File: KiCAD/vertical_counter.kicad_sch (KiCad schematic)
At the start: 14 parts, among them U10 74HC04, U12 74HC32, U15 74HC161, U16 74HC161, U17 74HC161, U18 74HC04, U19 74HC04, U20 74HC133, U21 74HC133, U22 74HC133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

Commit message: finished schematics and footprint assignments; need to figure out +5v connection issue
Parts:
- added unit 3 of U24
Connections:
- net +5V: now also U24.16 (VCC)
- net GND: now also U24.8 (GND)
- net j_addr4 renamed i_addr4
- net j_addr5 renamed i_addr5
- net j_addr6 renamed i_addr6
- net j_addr7 renamed i_addr7
- no-connect marks 4 -> 2
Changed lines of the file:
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@@
 	)
 	(junction
+		(at 255.27 30.48)
+		(diameter 0)
+		(color 0 0 0 0)
+	)
+	(junction
 		(at 77.47 162.56)
 		(diameter 0)
@@
 	)
 	(junction
+		(at 255.27 55.88)
+		(diameter 0)
+		(color 0 0 0 0)
+	)
+	(junction
 		(at 77.47 124.46)
 		(diameter 0)
@@
 	)
 	(no_connect
-		(at 154.94 134.62)
-	)
-	(no_connect
-		(at 151.13 138.43)
-	)
-	(no_connect
-		(at 151.13 172.72)
+		(at 168.91 175.26)
 	)
 	(no_connect
@@
 	(wire
 		(pts
+			(xy 255.27 30.48) (xy 270.51 30.48)
+		)
+		(stroke
+			(width 0)
+			(type default)
+		)
+	)
+	(wire
+		(pts
 			(xy 209.55 55.88) (xy 224.79 55.88)
 		)
@@
 	(wire
 		(pts
+			(xy 270.51 30.48) (xy 270.51 33.02)
+		)
+		(stroke
+			(width 0)
+			(type default)
+		)
+	)
+	(wire
+		(pts
 			(xy 179.07 55.88) (xy 194.31 55.88)
 		)
@@
 		)
 	)
+	(wire
+		(pts
+			(xy 270.51 53.34) (xy 270.51 55.88)
+		)
+		(stroke
+			(width 0)
+			(type default)
+		)
+	)
 	(bus
 		(pts
@@
 	(wire
 		(pts
+			(xy 270.51 55.88) (xy 255.27 55.88)
+		)
+		(stroke
+			(width 0)
+			(type default)
+		)
+	)
+	(wire
+		(pts
 			(xy 245.11 191.77) (xy 259.08 191.77)
 		)
@@
 		)
 	)
-	(label "j_addr5"
+	(label "i_addr5"
 		(at 245.11 194.31 0)
 		(effects
@@
 		)
 	)
-	(label "j_addr3"
+	(label "i_addr3"
 		(at 247.65 139.7 0)
 		(effects
@@
 		)
 	)
-	(label "j_addr0"
+	(label "i_addr0"
 		(at 247.65 132.08 0)
 		(effects
@@
 		)
 	)
-	(label "j_addr1"
+	(label "i_addr1"
 		(at 247.65 134.62 0)
 		(effects
@@
 		)
 	)
-	(label "j_addr2"
+	(label "i_addr2"
 		(at 247.65 137.16 0)
 		(effects
@@
 		)
 	)
-	(label "j_addr4"
+	(label "i_addr4"
 		(at 245.11 191.77 0)
 		(effects
@@
 		)
 	)
-	(label "j_addr7"
+	(label "i_addr7"
 		(at 245.11 199.39 0)
 		(effects
@@
 		)
 	)
-	(label "j_addr6"
+	(label "i_addr6"
 		(at 245.11 196.85 0)
 		(effects
@@
 		)
 	)
-	(hierarchical_label "j_addr[0..7]"
+	(hierarchical_label "i_addr[0..7]"
 		(shape output)
 		(at 290.83 201.93 0)
@@
 				)
 			)
+		)
+	)
+	(symbol
+		(lib_id "74xx:74LS112")
+		(at 270.51 43.18 0)
+		(unit 3)
+		(exclude_from_sim no)
+		(in_bom yes)
+		(on_board yes)
+		(dnp no)
+		(fields_autoplaced yes)
+		(property "Reference" "U24"
+			(at 272.6533 33.02 0)
+			(effects
+				(font
+					(size 1.27 1.27)
+				)
+				(justify left)
+			)
+		)
+		(property "Value" "74HC112"
+			(at 272.6533 35.56 0)
+			(effects
+				(font
+					(size 1.27 1.27)
+				)
+				(justify left)
+			)
+		)
+		(property "Footprint" "Package_DIP:DIP-16_W7.62mm"
+			(at 270.51 43.18 0)
+			(effects
+				(font
+					(size 1.27 1.27)
+				)
+				(hide yes)
+			)
+		)
+		(property "Datasheet" "http://www.ti.com/lit/gpn/sn74LS112"
+			(at 270.51 43.18 0)
+			(effects
+				(font
+					(size 1.27 1.27)
+				)
+				(hide yes)
+			)
+		)
+		(property "Description" "dual JK Flip-Flop, Set & Reset"
+			(at 270.51 43.18 0)
+			(effects
+				(font
+					(size 1.27 1.27)
+				)
+				(hide yes)
+			)
+		)
+		(pin "1"
+		)
+		(pin "12"
+		)
+		(pin "5"
+		)
+		(pin "3"
+		)
+		(pin "15"
+		)
+		(pin "2"
+		)
+		(pin "11"
+		)
+		(pin "4"
+		)
+		(pin "10"
+		)
+		(pin "14"
+		)
+		(pin "7"
+		)
+		(pin "6"
+		)
+		(pin "13"
+		)
+		(pin "8"
+		)
+		(pin "16"
+		)
+		(pin "9"
+		)
+		(instances
+			(project "vga_video_card"
+				(path "/53ebbfbe-eaa1-4706-acc1-611a99db7179/318d78f1-f69a-43bc-862b-642862639a11"
+					(reference "U24")
+					(unit 3)
+				)
+			)

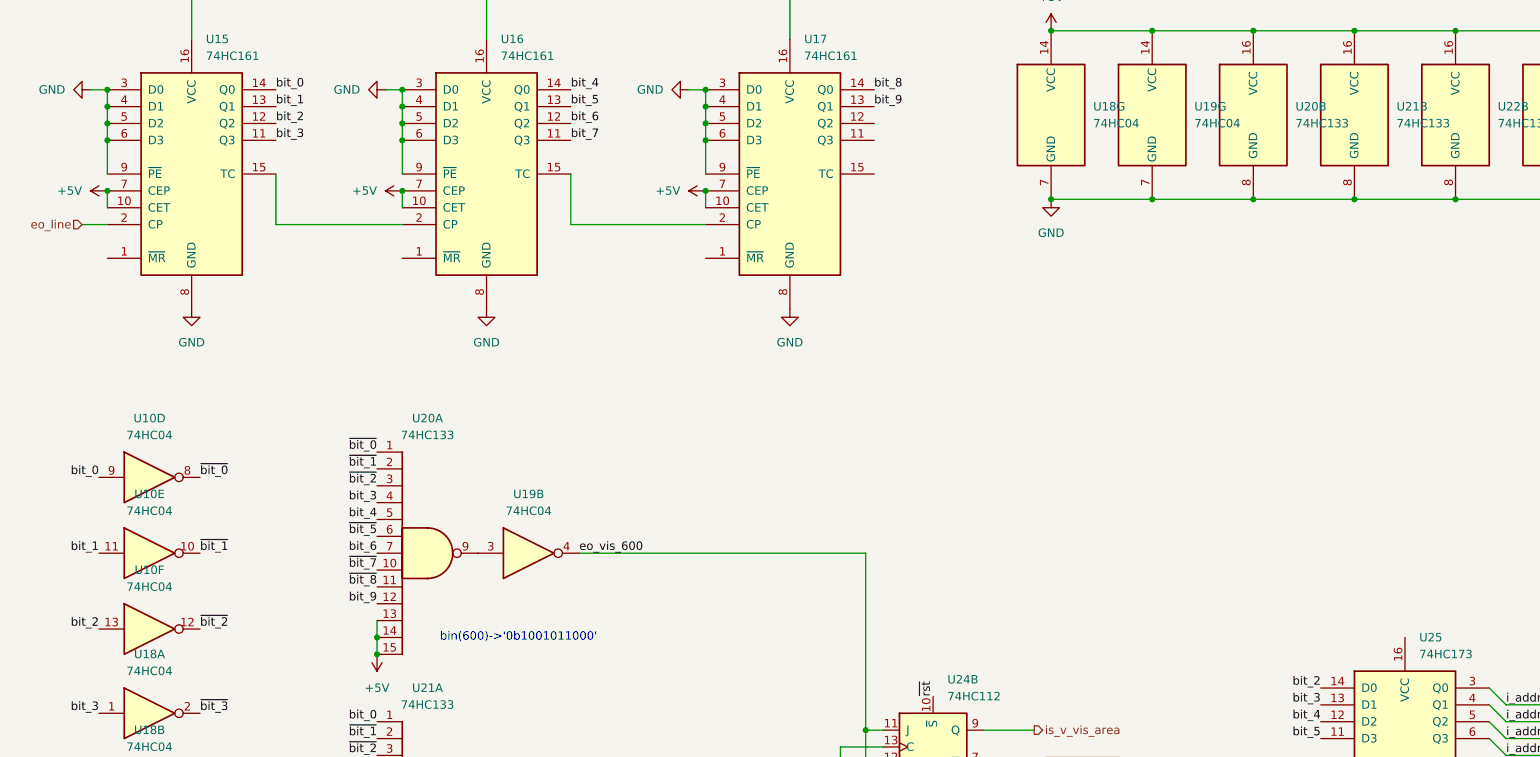
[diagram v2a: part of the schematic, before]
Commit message: fix multiple ERCs that made RAM addrs not connecting
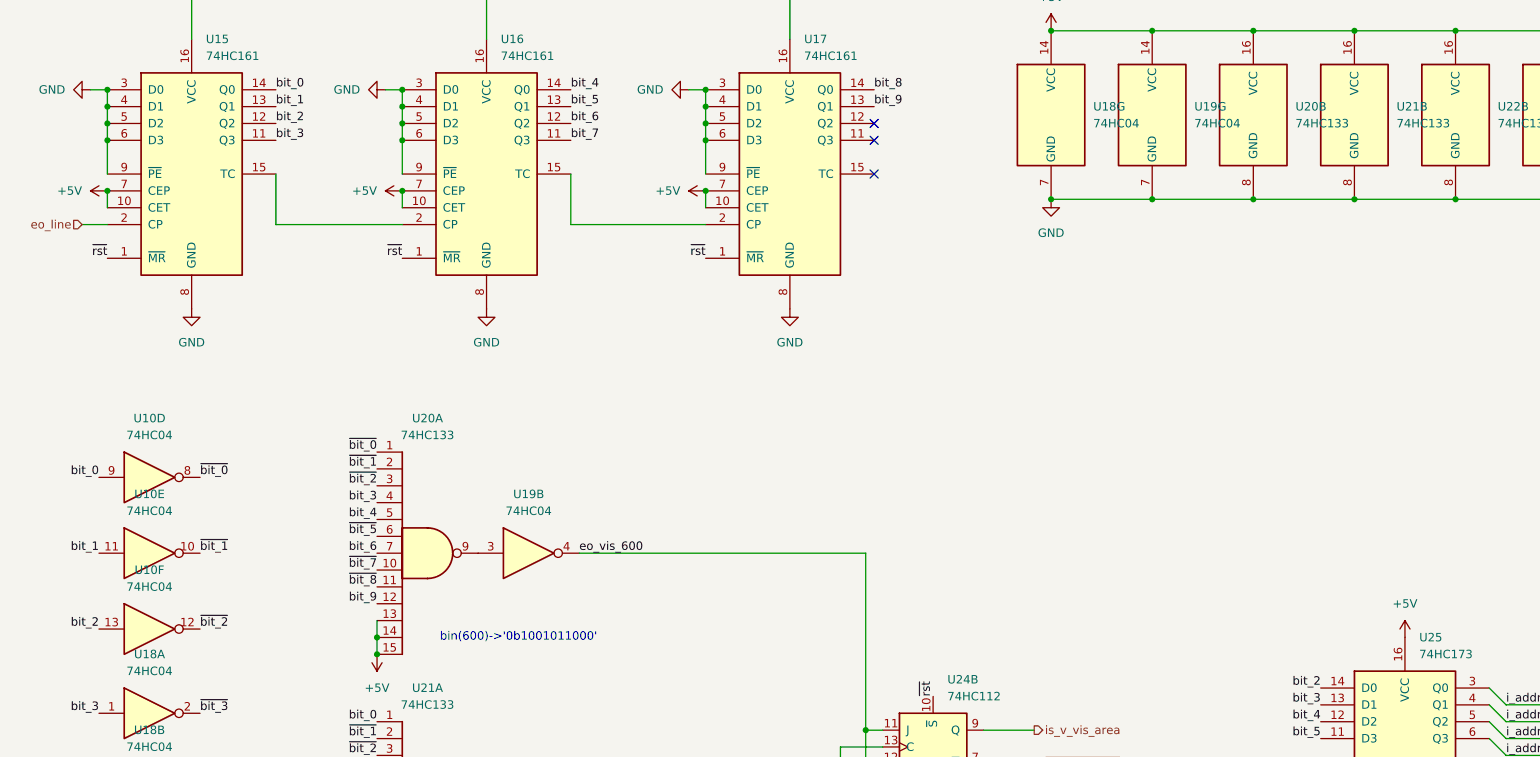
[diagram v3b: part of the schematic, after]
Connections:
- net +5V: now also U25.16 (VCC)
- net ~{rst}: now also U15.1 (~{MR}), U16.1 (~{MR}), U17.1 (~{MR})
- no-connect marks 2 -> 5
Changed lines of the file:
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@@
 	)
 	(no_connect
+		(at 152.4 44.45)
+	)
+	(no_connect
+		(at 152.4 52.07)
+	)
+	(no_connect
+		(at 152.4 46.99)
+	)
+	(no_connect
 		(at 222.25 209.55)
 	)
@@
 		)
 	)
+	(label "~{rst}"
+		(at 81.28 64.77 180)
+		(effects
+			(font
+				(size 1.27 1.27)
+			)
+			(justify right bottom)
+		)
+	)
 	(label "bit_0"
 		(at 77.47 176.53 180)
@@
 		)
 	)
+	(label "~{rst}"
+		(at 36.83 64.77 180)
+		(effects
+			(font
+				(size 1.27 1.27)
+			)
+			(justify right bottom)
+		)
+	)
 	(label "bit_8"
 		(at 219.71 196.85 180)
@@
 		)
 	)
+	(label "~{rst}"
+		(at 127 64.77 180)
+		(effects
+			(font
+				(size 1.27 1.27)
+			)
+			(justify right bottom)
+		)
+	)
 	(label "bit_6"
 		(at 106.68 44.45 0)
@@
 					(unit 1)
 				)
+			)
+		)
+	)
+	(symbol
+		(lib_id "power:+5V")
+		(at 232.41 121.92 0)
+		(unit 1)
+		(exclude_from_sim no)
+		(in_bom yes)
+		(on_board yes)
+		(dnp no)
+		(fields_autoplaced yes)
+		(property "Reference" "#PWR0119"
+			(at 232.41 125.73 0)
+			(effects
+				(font
+					(size 1.27 1.27)
+				)
+				(hide yes)
+			)
+		)
+		(property "Value" "+5V"
+			(at 232.41 116.84 0)
+			(effects
+				(font
+					(size 1.27 1.27)
+				)
+			)
+		)
+		(property "Footprint" ""
+			(at 232.41 121.92 0)
+			(effects
+				(font
+					(size 1.27 1.27)
+				)
+				(hide yes)
+			)
+		)
+		(property "Datasheet" ""
+			(at 232.41 121.92 0)
+			(effects
+				(font
+					(size 1.27 1.27)
+				)
+				(hide yes)
+			)
+		)
+		(property "Description" "Power symbol creates a global label with name \"+5V\""
+			(at 232.41 121.92 0)
+			(effects
+				(font
+					(size 1.27 1.27)
+				)
+				(hide yes)
+			)
+		)
+		(pin "1"
+		)
+		(instances
+			(project ""
+				(path "/53ebbfbe-eaa1-4706-acc1-611a99db7179/318d78f1-f69a-43bc-862b-642862639a11"
+					(reference "#PWR0119")
+					(unit 1)
+				)

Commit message: clean up; resolve ERC warnings
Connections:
- net i_addr0: now also U25.3 (Q0)
- net i_addr1: now also U25.4 (Q1)
- net i_addr2: now also U25.5 (Q2)
- net i_addr3: now also U25.6 (Q3)

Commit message: resolved most ERC errors
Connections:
- no-connect marks 5 -> 4
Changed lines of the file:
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@@
 		(at 152.4 46.99)
-	)
-	(no_connect
-		(at 222.25 209.55)
 	)
 	(bus_entry

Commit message: updated KiCAD todos
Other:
- note added: "TODO: PE should be disabled"
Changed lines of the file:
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@@
+		)
+	)
+	(text "TODO: PE should be disabled"
+		(exclude_from_sim no)
+		(at 29.464 28.956 0)
+		(effects
+			(font
+				(size 1.27 1.27)
+			)
 		)
 	)

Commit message: schematics disabled PE
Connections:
- net +5V: now also U15.9 (~{PE}), U16.9 (~{PE}), U17.9 (~{PE})
- net GND: no longer U15.9 (~{PE}), U16.9 (~{PE}), U17.9 (~{PE})
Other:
- note removed: "TODO: PE should be disabled"
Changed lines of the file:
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@@
-		)
-	)
-	(text "TODO: PE should be disabled"
-		(exclude_from_sim no)
-		(at 29.464 28.956 0)
-		(effects
-			(font
-				(size 1.27 1.27)
-			)
 		)
 	)
@@
 	)
 	(junction
-		(at 81.28 46.99)
-		(diameter 0)
-		(color 0 0 0 0)
-	)
-	(junction
-		(at 36.83 46.99)
-		(diameter 0)
-		(color 0 0 0 0)
-	)
-	(junction
 		(at 224.79 30.48)
 		(diameter 0)
@@
 	(junction
 		(at 219.71 205.74)
-		(diameter 0)
-		(color 0 0 0 0)
-	)
-	(junction
-		(at 127 46.99)
 		(diameter 0)
 		(color 0 0 0 0)
@@
 	(wire
 		(pts
+			(xy 127 52.07) (xy 127 54.61)
+		)
+		(stroke
+			(width 0)
+			(type default)
+		)
+	)
+	(wire
+		(pts
 			(xy 245.11 134.62) (xy 259.08 134.62)
 		)
@@
 	(wire
 		(pts
-			(xy 81.28 46.99) (xy 81.28 52.07)
-		)
-		(stroke
-			(width 0)
-			(type default)
-		)
-	)
-	(wire
-		(pts
 			(xy 144.78 172.72) (xy 147.32 172.72)
 		)
@@
 		)
 	)
+	(wire
+		(pts
+			(xy 81.28 52.07) (xy 81.28 54.61)
+		)
+		(stroke
+			(width 0)
+			(type default)
+		)
+	)
 	(bus
 		(pts
@@
 	(wire
 		(pts
-			(xy 36.83 46.99) (xy 36.83 52.07)
-		)
-		(stroke
-			(width 0)
-			(type default)
-		)
-	)
-	(wire
-		(pts
 			(xy 219.71 204.47) (xy 219.71 205.74)
 		)
@@
 	(wire
 		(pts
-			(xy 127 46.99) (xy 127 52.07)
-		)
-		(stroke
-			(width 0)
-			(type default)
-		)
-	)
-	(wire
-		(pts
 			(xy 147.32 138.43) (xy 153.67 138.43)
 		)
@@
 		)
 		(stroke
+			(width 0)
+			(type default)
+		)
+	)
+	(wire
+		(pts
+			(xy 36.83 52.07) (xy 36.83 54.61)
+		)
+		(stroke
